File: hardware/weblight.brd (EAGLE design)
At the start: 38.1 x 12.7 mm, 19 parts, among them U1 ATtiny85-20SU

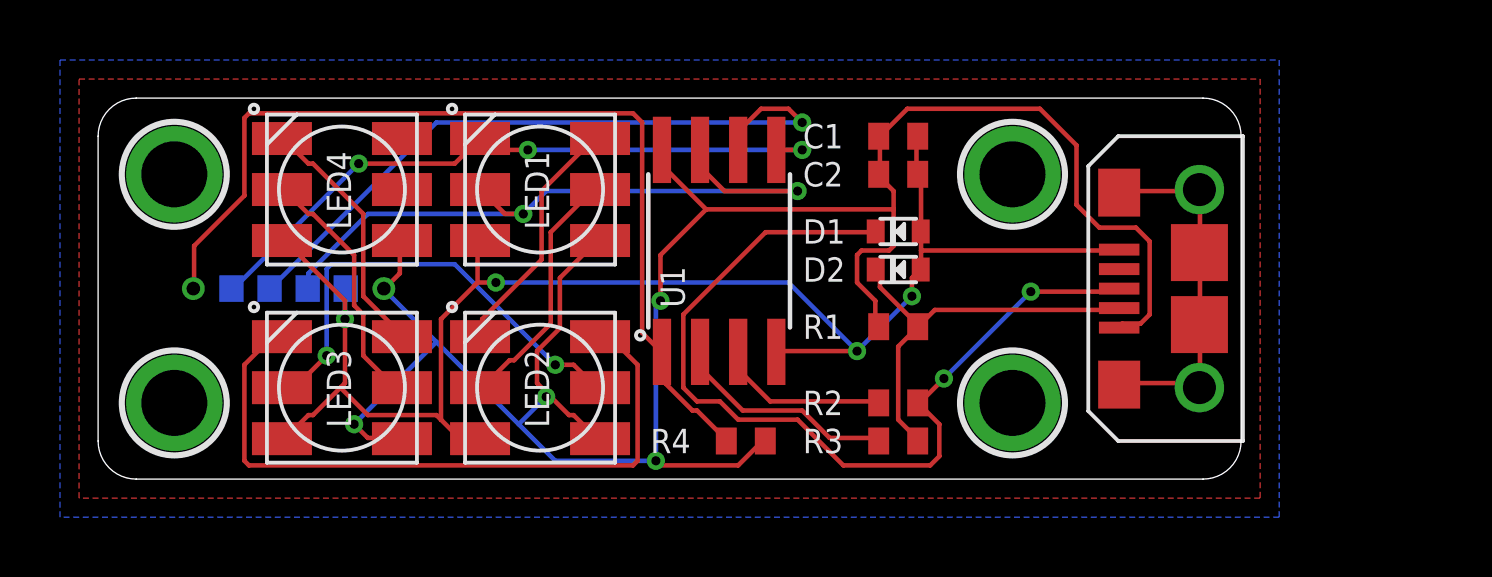
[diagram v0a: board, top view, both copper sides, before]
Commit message: mf2 production 0805 - ordered from OSH & Seeed
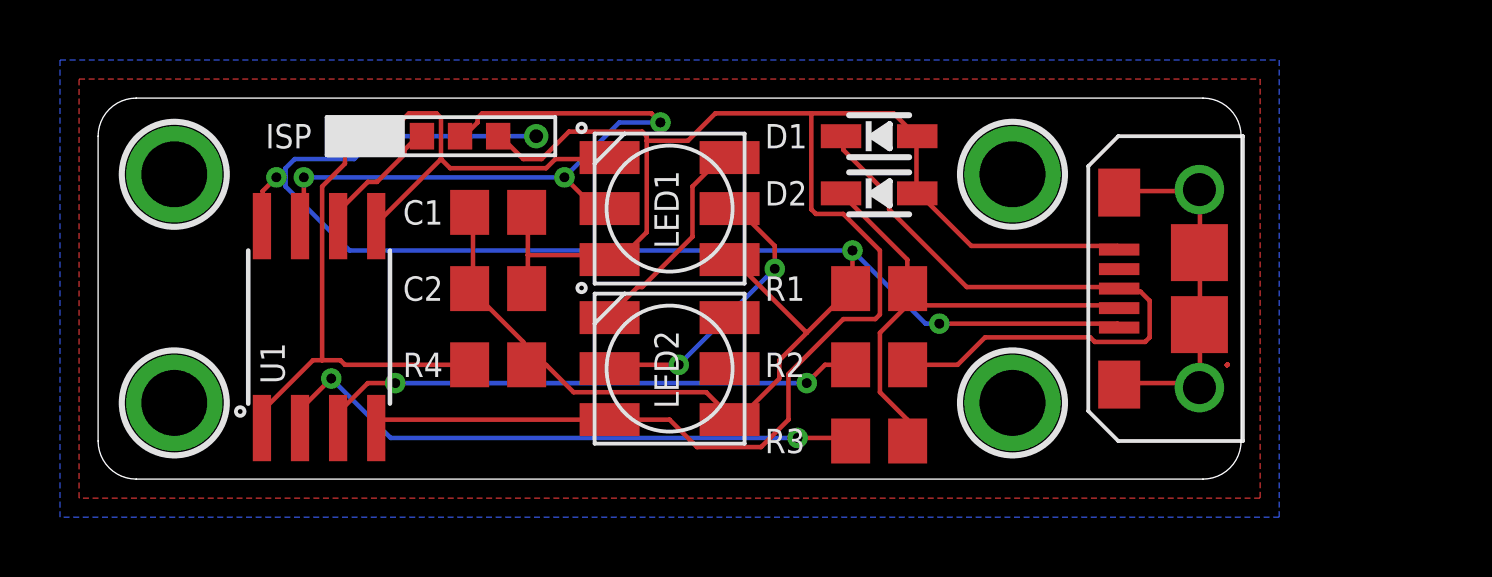
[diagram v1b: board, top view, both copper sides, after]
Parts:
- removed ICSP: POGOPIN-CONNWITHVIAS, weblight:POGOPROG-CONN-0H
- removed LED3, LED4: APA102, weblight:APA102
- added ISP: POGOPIN-CONNWITHVIAS, weblight:POGOPROG-CONN-0H
- C1, C2: device rcl:C0402 -> rcl:C0805
- D1, D2: device microbuilder:SOD-523 -> microbuilder:SOD-323
- R1, R2, R3: device rcl:R0402 -> rcl:R0805
- R4: value 4.7K -> 10K; device rcl:R0402 -> rcl:R0805
- moved C2 13.9 mm to (13.3, 6.35)
- moved C1 13.6 mm to (13.3, 8.89)
- moved U1 13.6 mm to (7.37, 5.08)
- moved R4 8.64 mm to (13.3, 3.81)
- moved LED1 4.36 mm to (19.1, 9.02)
- moved LED2 4.36 mm to (19.1, 3.68)
- moved D1 3.24 mm to (26.0, 11.4), turned to 0 degrees
- moved D2 2.62 mm to (26.0, 9.53), turned to 0 degrees
- moved R2 1.42 mm to (26.0, 3.81)
- moved R1 1.42 mm to (26.0, 6.35)
- moved R3 0.64 mm to (26.0, 1.27)
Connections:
- removed net CLK_3: LED2.CO, LED3.CI
- removed net CLK_4: LED3.CO, LED4.CI
- removed net DIN_3: LED2.DO, LED3.DI
- removed net DIN_4: LED3.DO, LED4.DI
- net CLK_1/SCK: now also ISP.4; no longer ICSP.4
- net DIN_1/MOSI: now also ISP.2; no longer ICSP.2
- net GND: now also ISP.5; no longer ICSP.5, LED3.GND, LED4.GND
- net MISO: now also ISP.3; no longer ICSP.3
- net N_RESET: now also ISP.1; no longer ICSP.1
- net USB_D_MINUS_RAW: now also D2.C; no longer D2.K
- net USB_D_PLUS_RAW: now also D1.C; no longer D1.K
- net VCC: now also ISP.6; no longer ICSP.6, LED3.VCC, LED4.VCC
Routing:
- net DIN_3: track 22.9 -> 0.00 mm
- net MISO: track 23.3 -> 4.40 mm, vias 1 -> 0
- net CLK_3: track 15.7 -> 0.00 mm, vias 2 -> 0
- net N_RESET: track 31.7 -> 16.1 mm
- net USB_D_MINUS: track 7.48 -> 20.3 mm, vias 0 -> 2
- net USB_D_PLUS: track 5.72 -> 18.2 mm, vias 0 -> 2
- net GND: track 52.5 -> 63.4 mm, vias 4 -> 0
- net DIN_1/MOSI: track 22.1 -> 12.7 mm, vias 3 -> 0
- net VCC: track 75.0 -> 66.1 mm, vias 4 -> 3
- net CLK_4: track 8.51 -> 0.00 mm
- net DIN_4: track 8.36 -> 0.00 mm
- net USB_D_PLUS_RAW: track 30.1 -> 22.9 mm, vias 2 -> 0
- net USB_D_MINUS_RAW: track 13.8 -> 17.5 mm
- net CLK_2: track 8.60 -> 9.83 mm, vias 0 -> 2
- net DIN_2: track 8.42 -> 7.25 mm
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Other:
- board text added: "mf2"
- board text removed: "a-mf1"

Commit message: Connectorless USB, longer board. Unrouted.
  - Two diodes to protect back connector. Thanks Passerby
    http://electronics.stackexchange.com/q/209941/84391
  - Moved C1/C2 closer to where they matter.
  - A few astute layout changes to facilitate future routing.
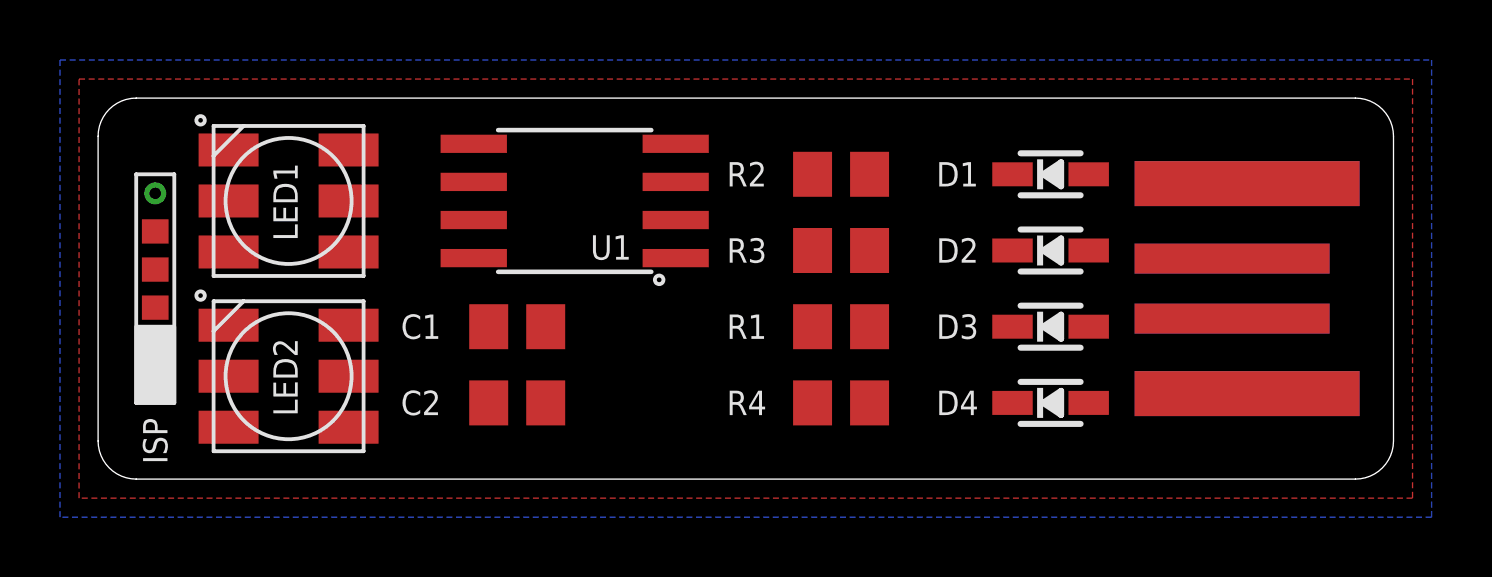
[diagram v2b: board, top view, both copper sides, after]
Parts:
- removed HOLE1, HOLE2, HOLE3, HOLE4: MOUNTINGHOLE2.0, microbuilder:MOUNTINGHOLE_2.0_PLATED
- removed JP-USB-MICRO: USB, MF_Connectors:MICROUSB-RIGHT
- added D3, D4: (no value), microbuilder:SOD-323
- added J-BOT, J-TOP: USBPCB_NOPASTE, SparkFun-Connectors:USB-A-PCB-NOPASTE
- D1, D2: value 3.6V -> 3.6V Zener
- ISP: value POGOPIN-CONNWITHVIAS -> POGOPIN-CONNWITHVIAS-SMV; device weblight:POGOPROG-CONN-0H -> weblight:POGOPROG-CONN-OH-SMALLERVIAS
- moved LED1 12.7 mm to (6.35, 9.27)
- moved LED2 12.7 mm to (6.35, 3.43)
- moved ISP 11.7 mm to (1.91, 5.71), turned to 180 degrees
- moved R4 11.5 mm to (24.8, 2.54)
- moved U1 9.49 mm to (15.9, 9.27), turned to 90 degrees
- moved R2 6.48 mm to (24.8, 10.2)
- moved R3 6.48 mm to (24.8, 7.62)
- moved D2 6.02 mm to (31.8, 7.62)
- moved D1 5.85 mm to (31.8, 10.2)
- moved C1 3.86 mm to (14.0, 5.08), turned to 0 degrees
- moved C2 3.86 mm to (14.0, 2.54), turned to 0 degrees
- moved R1 1.80 mm to (24.8, 5.08)
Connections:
- removed net SLD: JP-USB-MICRO.S1, JP-USB-MICRO.S2, JP-USB-MICRO.S3, JP-USB-MICRO.S4, JP-USB-MICRO.S5, JP-USB-MICRO.S6
- new net 5V: D3.A, D4.A, J-BOT.5V, J-TOP.5V
- net GND: now also J-BOT.GND, J-TOP.GND; no longer JP-USB-MICRO.5
- net USB_D_MINUS_RAW: now also J-BOT.USB_M, J-TOP.USB_M, R1.1; no longer JP-USB-MICRO.2, R1.2
- net USB_D_PLUS_RAW: now also J-BOT.USB_P, J-TOP.USB_P; no longer JP-USB-MICRO.3
- net VCC: now also D3.C, D4.C, R1.2; no longer JP-USB-MICRO.1, R1.1
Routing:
- net VCC: track 66.1 -> 0.00 mm, vias 3 -> 0
- net GND: track 63.4 -> 0.00 mm
- net CLK_1/SCK: track 23.5 -> 0.00 mm, vias 3 -> 0
- net USB_D_PLUS_RAW: track 22.9 -> 0.00 mm
- net USB_D_MINUS: track 20.3 -> 0.00 mm, vias 2 -> 0
- net USB_D_PLUS: track 18.2 -> 0.00 mm, vias 2 -> 0
- net USB_D_MINUS_RAW: track 17.5 -> 0.00 mm
- net N_RESET: track 16.1 -> 0.00 mm
- net DIN_1/MOSI: track 12.7 -> 0.00 mm
- net SLD: track 12.1 -> 0.00 mm
- net CLK_2: track 9.83 -> 0.00 mm, vias 2 -> 0
- net DIN_2: track 7.25 -> 0.00 mm
- net MISO: track 4.40 -> 0.00 mm
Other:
- board size 38.1 x 12.7 mm -> 43.2 x 12.7 mm
- board text added: "WebLight 0.9.1"
- board text added: "github.com/sowbug/weblight"
- board text removed: "WebLight"
- board text removed: "mf2"

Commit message: Checkpoint before routing
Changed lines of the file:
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@@
 <text x="21.59" y="6.35" size="2.54" layer="26" font="vector" rot="MR0" align="center">WebLight 0.9.1</text>
 <text x="21.59" y="3.175" size="1.016" layer="26" font="vector" rot="MR0" align="center">github.com/sowbug/weblight</text>
+<rectangle x1="34.29" y1="0" x2="43.18" y2="12.7" layer="43"/>
 </plain>
 <attributes>
@@
 <contactref element="D4" pad="C"/>
 <contactref element="D3" pad="C"/>
-<wire x1="30.48" y1="5.08" x2="30.48" y2="2.54" width="0" layer="19" extent="1-1"/>
-<wire x1="1.905" y1="9.525" x2="30.48" y2="5.08" width="0" layer="19" extent="1-1"/>
-<wire x1="8.35" y1="7.571" x2="1.905" y2="9.525" width="0" layer="19" extent="1-1"/>
-<wire x1="12.5222" y1="7.366" x2="8.35" y2="7.571" width="0" layer="19" extent="1-1"/>
-<wire x1="14.92" y1="5.08" x2="12.5222" y2="7.366" width="0" layer="19" extent="1-1"/>
+<wire x1="30.48" y1="2.54" x2="30.48" y2="5.08" width="0" layer="19" extent="1-1"/>
+<wire x1="25.715" y1="5.08" x2="30.48" y2="5.08" width="0" layer="19" extent="1-1"/>
+<wire x1="25.715" y1="2.54" x2="25.715" y2="5.08" width="0" layer="19" extent="1-1"/>
+<wire x1="14.92" y1="5.08" x2="25.715" y2="5.08" width="0" layer="19" extent="1-1"/>
 <wire x1="14.92" y1="2.54" x2="14.92" y2="5.08" width="0" layer="19" extent="1-1"/>
-<wire x1="8.35" y1="1.729" x2="14.92" y2="2.54" width="0" layer="19" extent="1-1"/>
-<wire x1="25.715" y1="5.08" x2="14.92" y2="5.08" width="0" layer="19" extent="1-1"/>
-<wire x1="25.715" y1="2.54" x2="25.715" y2="5.08" width="0" layer="19" extent="1-1"/>
+<wire x1="12.5222" y1="7.366" x2="14.92" y2="5.08" width="0" layer="19" extent="1-1"/>
+<wire x1="8.35" y1="7.571" x2="12.5222" y2="7.366" width="0" layer="19" extent="1-1"/>
+<wire x1="8.35" y1="1.729" x2="8.35" y2="7.571" width="0" layer="19" extent="1-1"/>
+<wire x1="1.905" y1="9.525" x2="8.35" y2="7.571" width="0" layer="19" extent="1-1"/>
 </signal>
 <signal name="GND">
@@
 </polygon>
 <contactref element="J-BOT" pad="GND"/>
-<wire x1="33.02" y1="7.62" x2="33.02" y2="10.16" width="0" layer="19" extent="1-1"/>
-<wire x1="38.3" y1="2.85" x2="33.02" y2="7.62" width="0" layer="19" extent="1-1"/>
-<wire x1="19.2532" y1="11.176" x2="33.02" y2="10.16" width="0" layer="19" extent="1-1"/>
-<wire x1="13.02" y1="5.08" x2="19.2532" y2="11.176" width="0" layer="19" extent="1-1"/>
-<wire x1="13.02" y1="2.54" x2="13.02" y2="5.08" width="0" layer="19" extent="1-1"/>
-<wire x1="4.35" y1="1.729" x2="13.02" y2="2.54" width="0" layer="19" extent="1-1"/>
-<wire x1="4.35" y1="7.571" x2="4.35" y2="1.729" width="0" layer="19" extent="1-1"/>
-<wire x1="1.905" y1="8.255" x2="4.35" y2="7.571" width="0" layer="19" extent="1-1"/>
-<wire x1="38.3" y1="9.85" x2="1.905" y2="8.255" width="0" layer="19" extent="1-1"/>
+<via x="17.145" y="10.795" extent="1-16" drill="0.381"/>
 </signal>
 <signal name="USB_D_MINUS">
@@
 <contactref element="J-TOP" pad="USB_M"/>
 <contactref element="J-BOT" pad="USB_M"/>
+<wire x1="37.8" y1="5.35" x2="37.8" y2="7.35" width="0" layer="19" extent="1-16"/>
 <wire x1="30.48" y1="7.62" x2="37.8" y2="7.35" width="0" layer="19" extent="1-1"/>
 <wire x1="25.715" y1="7.62" x2="30.48" y2="7.62" width="0" layer="19" extent="1-1"/>
 <wire x1="23.815" y1="5.08" x2="25.715" y2="7.62" width="0" layer="19" extent="1-1"/>
-<wire x1="37.8" y1="5.35" x2="23.815" y2="5.08" width="0" layer="19" extent="1-1"/>
 </signal>
 <signal name="USB_D_PLUS_RAW">
@@
 <contactref element="J-TOP" pad="USB_P"/>
 <contactref element="J-BOT" pad="USB_P"/>
-<wire x1="30.48" y1="10.16" x2="37.8" y2="5.35" width="0" layer="19" extent="1-1"/>
 <wire x1="25.715" y1="10.16" x2="30.48" y2="10.16" width="0" layer="19" extent="1-1"/>
-<wire x1="37.8" y1="7.35" x2="25.715" y2="10.16" width="0" layer="19" extent="1-1"/>
+<wire x1="37.8" y1="7.35" x2="30.48" y2="10.16" width="0" layer="19" extent="1-16"/>
+<wire x1="37.8" y1="5.35" x2="37.8" y2="7.35" width="0" layer="19" extent="1-16"/>
 </signal>
 <signal name="USB_D_PLUS">
@@
 <contactref element="D4" pad="A"/>
 <wire x1="38.3" y1="2.85" x2="38.3" y2="9.85" width="0" layer="19" extent="1-16"/>
-<wire x1="33.02" y1="5.08" x2="38.3" y2="2.85" width="0" layer="19" extent="1-16"/>
-<wire x1="33.02" y1="2.54" x2="33.02" y2="5.08" width="0" layer="19" extent="1-1"/>
+<wire x1="33.02" y1="2.54" x2="38.3" y2="2.85" width="0" layer="19" extent="1-16"/>
+<wire x1="33.02" y1="5.08" x2="33.02" y2="2.54" width="0" layer="19" extent="1-1"/>
 </signal>
 </signals>

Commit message: Some manual routing. Mess
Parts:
- moved D2 5.43 mm to (29.8, 2.54)
- moved D4 5.43 mm to (29.8, 7.62)
- moved D1 1.91 mm to (29.8, 10.2)
- moved D3 1.91 mm to (29.8, 5.08)
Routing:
- net VCC: track 0.00 -> 59.4 mm
- net USB_D_MINUS_RAW: track 0.00 -> 28.7 mm, vias 0 -> 1
- net N_RESET: track 0.00 -> 26.8 mm, vias 0 -> 1
- net USB_D_PLUS_RAW: track 0.00 -> 21.2 mm, vias 0 -> 2
- net DIN_1/MOSI: track 0.00 -> 20.5 mm
- net 5V: track 0.00 -> 18.6 mm, vias 0 -> 1
- net MISO: track 0.00 -> 14.8 mm, vias 0 -> 2
- net CLK_1/SCK: track 0.00 -> 12.9 mm, vias 0 -> 2
- net CLK_2: track 0.00 -> 10.2 mm, vias 0 -> 2
- net DIN_2: track 0.00 -> 8.39 mm, vias 0 -> 2
- net USB_D_MINUS: track 0.00 -> 5.17 mm
- net USB_D_PLUS: track 0.00 -> 4.67 mm

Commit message: Better initial layout. Unrouted
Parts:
- moved C1 2.54 mm to (14.0, 2.54)
- moved C2 2.54 mm to (14.0, 5.08)
- moved R1 2.54 mm to (24.8, 2.54)
- moved R4 2.54 mm to (24.8, 5.08)
- moved ISP 0.63 mm to (1.91, 6.35), turned to 0 degrees
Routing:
- net VCC: track 59.4 -> 0.00 mm
- net USB_D_MINUS_RAW: track 28.7 -> 0.00 mm, vias 1 -> 0
- net N_RESET: track 26.8 -> 0.00 mm, vias 1 -> 0
- net USB_D_PLUS_RAW: track 21.2 -> 0.00 mm, vias 2 -> 0
- net DIN_1/MOSI: track 20.5 -> 0.00 mm
- net 5V: track 18.6 -> 0.00 mm, vias 1 -> 0
- net MISO: track 14.8 -> 0.00 mm, vias 2 -> 0
- net CLK_1/SCK: track 12.9 -> 0.00 mm, vias 2 -> 0
- net CLK_2: track 10.2 -> 0.00 mm, vias 2 -> 0
- net DIN_2: track 8.39 -> 0.00 mm, vias 2 -> 0
- net USB_D_MINUS: track 5.17 -> 0.00 mm
- net USB_D_PLUS: track 4.67 -> 0.00 mm

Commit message: Got most of easy stuff routed.
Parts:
- turned C1 to 180 degrees
- turned C2 to 180 degrees
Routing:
- net VCC: track 0.00 -> 47.3 mm
- net DIN_1/MOSI: track 0.00 -> 18.5 mm
- net CLK_2: track 0.00 -> 10.1 mm
- net DIN_2: track 0.00 -> 9.87 mm
- net N_RESET: track 0.00 -> 6.85 mm
- net CLK_1/SCK: track 0.00 -> 6.64 mm
- net USB_D_MINUS: track 0.00 -> 5.58 mm
- net USB_D_PLUS: track 0.00 -> 4.82 mm
- net USB_D_PLUS_RAW: track 0.00 -> 2.86 mm
- net USB_D_MINUS_RAW: track 0.00 -> 1.14 mm
